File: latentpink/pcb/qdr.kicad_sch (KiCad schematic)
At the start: 69 parts, among them U2 XC7K160T-2FBG484C, U28 IS25WP256D-JLLE, U29 DSC1123CI2-150.0000T, U3 CY7C2245KV18-450BZXI

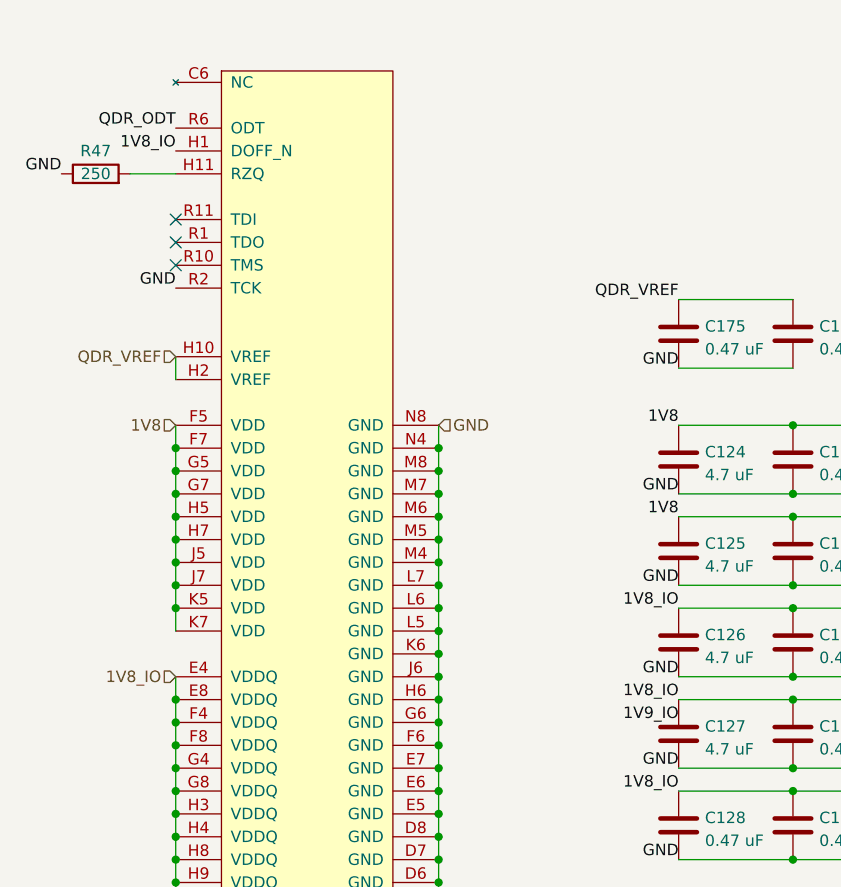
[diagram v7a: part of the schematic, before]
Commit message: Finished initial schematic, ready for design review
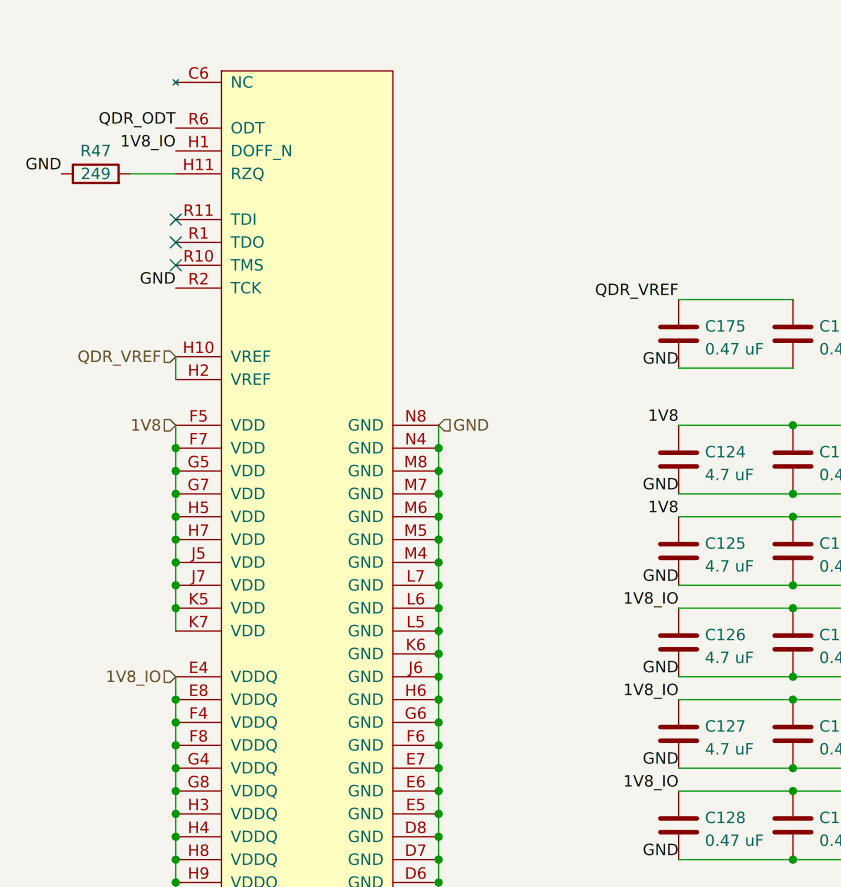
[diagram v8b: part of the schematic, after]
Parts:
- C177, C178: footprint (none) -> azonenberg_pcb:EIA_1206_CAP_NOSILK
- R47: value 250 -> 249; footprint (none) -> azonenberg_pcb:EIA_0402_RES_NOSILK
- RN1, RN2, RN3, RN4, RN5, RN6: footprint (none) -> azonenberg_pcb:YAGEO_YC124-FR
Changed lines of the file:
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@@
     (effects (font (size 1.27 1.27)) (justify right bottom))
   )
-  (label "1V9_IO" (at 88.9 232.41 180)
-    (effects (font (size 1.27 1.27)) (justify right bottom))
-  )
   (label "FPGA_FLASH_DQ1" (at 269.24 30.48 180)
     (effects (font (size 1.27 1.27)) (justify right bottom))
@@
       (effects (font (size 1.27 1.27)) (justify left))
     )
-    (property "Footprint" "" (id 2) (at 232.7402 182.245 0)
+    (property "Footprint" "azonenberg_pcb:EIA_1206_CAP_NOSILK" (id 2) (at 232.7402 182.245 0)
       (effects (font (size 1.27 1.27)) hide)
     )
@@
     (pin "2")
   )
-  (symbol (lib_id "xilinx-azonenberg:XC7KxT-FBG484") (at 351.79 149.86 0) (unit 5)
+  (symbol (lib_name "XC7KxT-FBG484_1") (lib_id "xilinx-azonenberg:XC7KxT-FBG484") (at 351.79 149.86 0) (unit 5)
     (in_bom yes) (on_board yes)
     (property "Reference" "U2" (id 0) (at 351.79 153.67 0)
@@
     (pin "2")
   )
-  (symbol (lib_id "xilinx-azonenberg:XC7KxT-FBG484") (at 274.32 149.86 0) (unit 4)
+  (symbol (lib_name "XC7KxT-FBG484_2") (lib_id "xilinx-azonenberg:XC7KxT-FBG484") (at 274.32 149.86 0) (unit 4)
     (in_bom yes) (on_board yes)
     (property "Reference" "U2" (id 0) (at 274.32 152.4 0)
@@
     (property "Reference" "RN1" (id 0) (at 205.74 169.0202 90))
     (property "Value" "YC124-FR-0749R9L" (id 1) (at 199.39 171.45 90))
-    (property "Footprint" "" (id 2) (at 205.74 169.545 90)
+    (property "Footprint" "azonenberg_pcb:YAGEO_YC124-FR" (id 2) (at 205.74 169.545 90)
       (effects (font (size 1.27 1.27)) hide)
     )
@@
     (property "Reference" "RN6" (id 0) (at 205.74 254.1102 90))
     (property "Value" "YC124-FR-0749R9L" (id 1) (at 199.39 256.54 90))
-    (property "Footprint" "" (id 2) (at 205.74 254.635 90)
+    (property "Footprint" "azonenberg_pcb:YAGEO_YC124-FR" (id 2) (at 205.74 254.635 90)
       (effects (font (size 1.27 1.27)) hide)
     )
@@
     (property "Reference" "RN4" (id 0) (at 205.74 219.8202 90))
     (property "Value" "YC124-FR-0749R9L" (id 1) (at 199.39 222.25 90))
-    (property "Footprint" "" (id 2) (at 205.74 220.345 90)
+    (property "Footprint" "azonenberg_pcb:YAGEO_YC124-FR" (id 2) (at 205.74 220.345 90)
       (effects (font (size 1.27 1.27)) hide)
     )
@@
     (property "Reference" "RN3" (id 0) (at 205.74 203.3102 90))
     (property "Value" "YC124-FR-0749R9L" (id 1) (at 199.39 205.74 90))
-    (property "Footprint" "" (id 2) (at 205.74 203.835 90)
+    (property "Footprint" "azonenberg_pcb:YAGEO_YC124-FR" (id 2) (at 205.74 203.835 90)
       (effects (font (size 1.27 1.27)) hide)
     )
@@
     (property "Reference" "RN2" (id 0) (at 205.74 185.5302 90))
     (property "Value" "YC124-FR-0749R9L" (id 1) (at 199.39 187.325 90))
-    (property "Footprint" "" (id 2) (at 205.74 186.055 90)
+    (property "Footprint" "azonenberg_pcb:YAGEO_YC124-FR" (id 2) (at 205.74 186.055 90)
       (effects (font (size 1.27 1.27)) hide)
     )
@@
     (property "Reference" "RN5" (id 0) (at 205.74 236.3302 90))
     (property "Value" "YC124-FR-0749R9L" (id 1) (at 199.39 238.76 90))
-    (property "Footprint" "" (id 2) (at 205.74 236.855 90)
+    (property "Footprint" "azonenberg_pcb:YAGEO_YC124-FR" (id 2) (at 205.74 236.855 90)
       (effects (font (size 1.27 1.27)) hide)
     )
@@
     (in_bom yes) (on_board yes)
     (property "Reference" "R47" (id 0) (at 24.13 168.91 90))
-    (property "Value" "250" (id 1) (at 24.13 171.45 90))
-    (property "Footprint" "" (id 2) (at 24.13 173.228 90)
+    (property "Value" "249" (id 1) (at 24.13 171.45 90))
+    (property "Footprint" "azonenberg_pcb:EIA_0402_RES_NOSILK" (id 2) (at 24.13 173.228 90)
       (effects (font (size 1.27 1.27)) hide)
     )
@@
       (effects (font (size 1.27 1.27)) (justify left))
     )
-    (property "Footprint" "" (id 2) (at 244.8052 182.245 0)
+    (property "Footprint" "azonenberg_pcb:EIA_1206_CAP_NOSILK" (id 2) (at 244.8052 182.245 0)
       (effects (font (size 1.27 1.27)) hide)
     )
